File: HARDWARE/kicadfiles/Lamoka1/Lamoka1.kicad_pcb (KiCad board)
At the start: 2 copper layers, 61 parts, among them IC1 INA240A2DR, J1 2606-1108/010-000, J2 2606-1352, J3 USB_C_Receptacle_USB2.0_14P, J4 470531000, J5 2604-1103, J6 Male-Header, J7 Male-Header, SW1 B3F-4055, U1 RP2354A, U10 ADS7128IRTER, U2 AMS1117-3.3, U3 74AHCT1G125, U4 LM5122MH/NOPB, U7 TPS62160DSGR, U8 TMP235A2DBZR, U9 TMP235A2DBZR

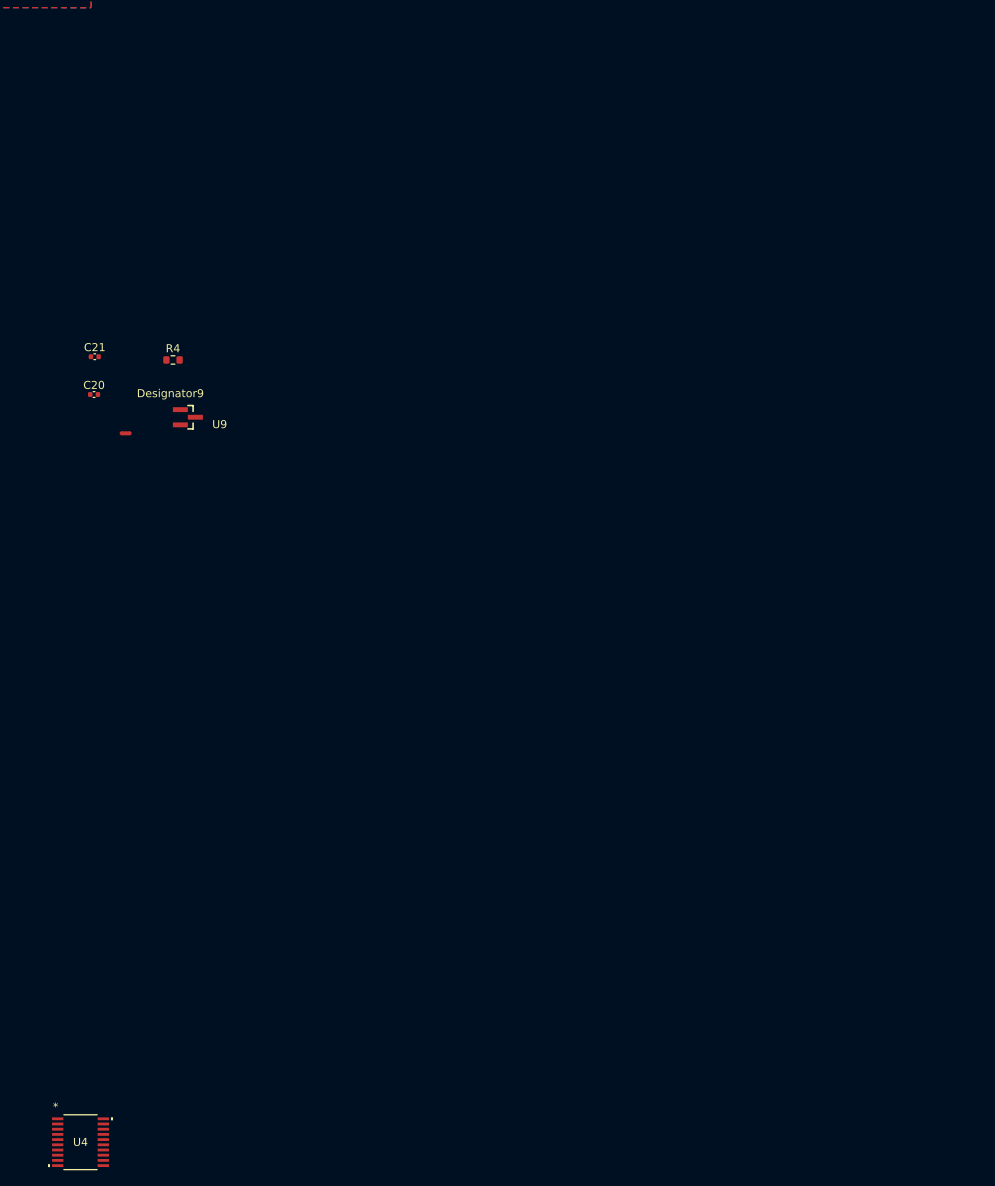
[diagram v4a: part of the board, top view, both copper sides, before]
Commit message: Route whole 11-14v to 17v boost converter
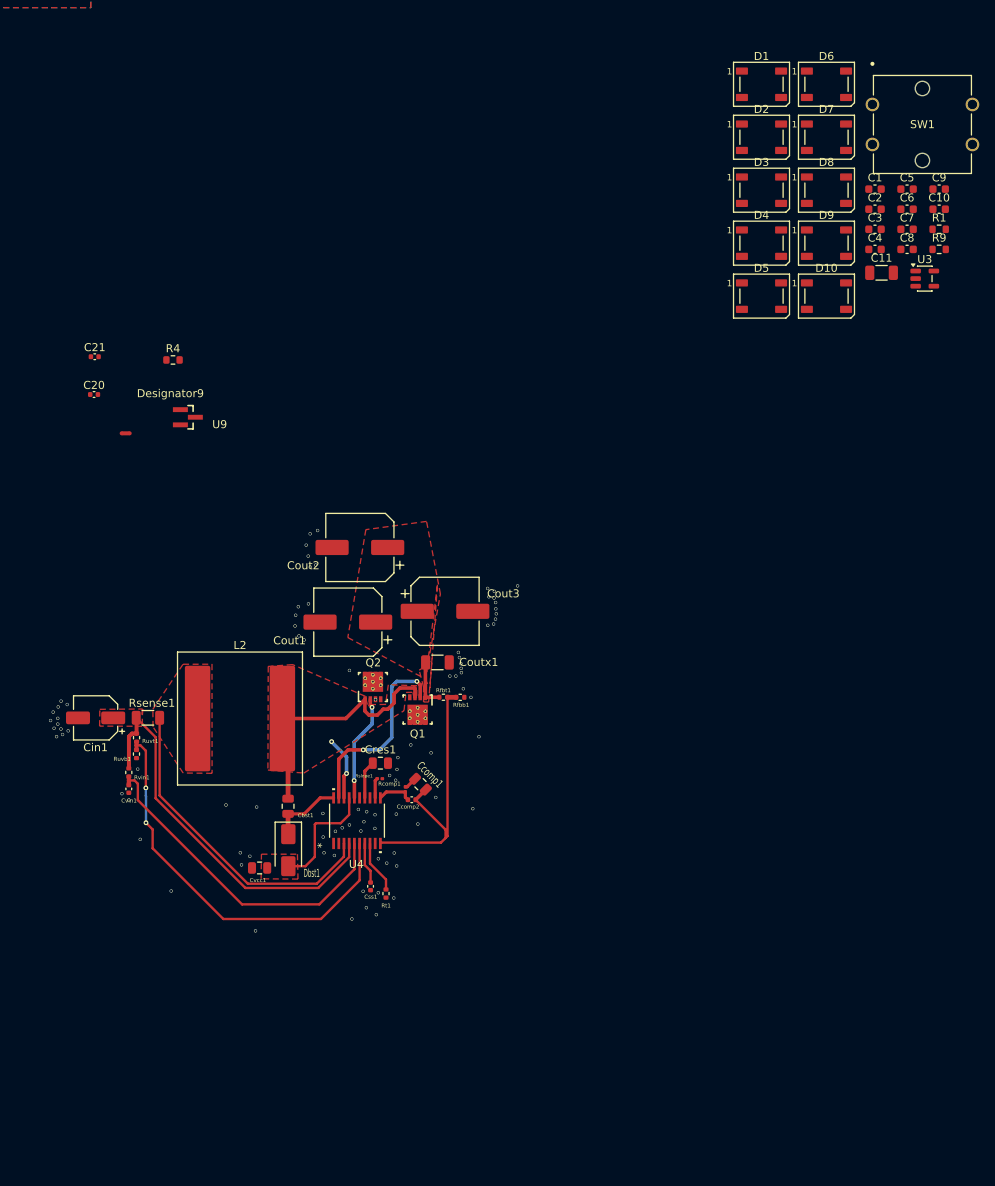
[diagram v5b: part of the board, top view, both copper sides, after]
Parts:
- added C1: 100n, Capacitor_SMD:C_0603_1608Metric, F.Cu at (246.3, 59.7)
- added C10: 100n, Capacitor_SMD:C_0603_1608Metric, F.Cu at (254.3, 62.2)
- added C11: 100u, Capacitor_SMD:C_1206_3216Metric, F.Cu at (247.1, 70.1)
- added C2: 100n, Capacitor_SMD:C_0603_1608Metric, F.Cu at (246.3, 62.2)
- added C3: 100n, Capacitor_SMD:C_0603_1608Metric, F.Cu at (246.3, 64.7)
- added C4: 100n, Capacitor_SMD:C_0603_1608Metric, F.Cu at (246.3, 67.2)
- added C5: 100n, Capacitor_SMD:C_0603_1608Metric, F.Cu at (250.3, 59.7)
- added C6: 100n, Capacitor_SMD:C_0603_1608Metric, F.Cu at (250.3, 62.2)
- added C7: 100n, Capacitor_SMD:C_0603_1608Metric, F.Cu at (250.3, 64.7)
- added C8: 100n, Capacitor_SMD:C_0603_1608Metric, F.Cu at (250.3, 67.2)
- added C9: 100n, Capacitor_SMD:C_0603_1608Metric, F.Cu at (254.3, 59.7)
- added Cbst1: 100nF, Capacitor_SMD:C_0805_2012Metric, F.Cu at (172.9, 136.8)
- added Ccomp1: 3.9nF, Capacitor_SMD:C_0805_2012Metric, F.Cu at (189.5, 134.0)
- added Ccomp2: 130pF, Capacitor_SMD:C_0402_1005Metric, F.Cu at (188.4, 136.0)
- added Cin1: 56uF, Capacitor_SMD:CP_Elec_5x5.9, F.Cu at (148.9, 125.8)
- added Cout1: 180uF, Capacitor_SMD:CP_Elec_8x11.9, F.Cu at (180.4, 113.8)
- added Cout2: 180uF, Capacitor_SMD:CP_Elec_8x11.9, F.Cu at (181.9, 104.5)
- added Cout3: 180uF, Capacitor_SMD:CP_Elec_8x11.9, F.Cu at (192.6, 112.4)
- added Coutx1: 47uF, Capacitor_SMD:C_1206_3216Metric, F.Cu at (191.6, 118.8)
- added Cres1: 470nF, Capacitor_SMD:C_0805_2012Metric, F.Cu at (184.5, 131.4)
- added Css1: 33nF, Capacitor_SMD:C_0402_1005Metric, F.Cu at (183.2, 146.8)
- added Cvcc1: 4.7uF, Capacitor_SMD:C_0805_2012Metric, F.Cu at (169.4, 144.5)
- added Cvin1: 470nF, Capacitor_SMD:C_0402_1005Metric, F.Cu at (153.0, 134.6)
- added D1: WS2812B, LED_SMD:LED_WS2812B_PLCC4_5.0x5.0mm_P3.2mm, F.Cu at (232.1, 46.5)
- added D10: WS2812B, LED_SMD:LED_WS2812B_PLCC4_5.0x5.0mm_P3.2mm, F.Cu at (240.2, 73.0)
- added D2: WS2812B, LED_SMD:LED_WS2812B_PLCC4_5.0x5.0mm_P3.2mm, F.Cu at (232.1, 53.2)
- added D3: WS2812B, LED_SMD:LED_WS2812B_PLCC4_5.0x5.0mm_P3.2mm, F.Cu at (232.1, 59.8)
- added D4: WS2812B, LED_SMD:LED_WS2812B_PLCC4_5.0x5.0mm_P3.2mm, F.Cu at (232.1, 66.4)
- added D5: WS2812B, LED_SMD:LED_WS2812B_PLCC4_5.0x5.0mm_P3.2mm, F.Cu at (232.1, 73.0)
- added D6: WS2812B, LED_SMD:LED_WS2812B_PLCC4_5.0x5.0mm_P3.2mm, F.Cu at (240.2, 46.5)
- added D7: WS2812B, LED_SMD:LED_WS2812B_PLCC4_5.0x5.0mm_P3.2mm, F.Cu at (240.2, 53.2)
- added D8: WS2812B, LED_SMD:LED_WS2812B_PLCC4_5.0x5.0mm_P3.2mm, F.Cu at (240.2, 59.8)
- added D9: WS2812B, LED_SMD:LED_WS2812B_PLCC4_5.0x5.0mm_P3.2mm, F.Cu at (240.2, 66.4)
- added Dbst1: D, Diode_SMD:D_SMA, F.Cu at (173.0, 142.3)
- added L2: 1.8uH, Inductor_SMD:L_Coilcraft_XAL1580-182, F.Cu at (166.9, 125.8)
- added Q1: 25V 60A N-Ch, CSD16323Q3:DQG0008A, F.Cu at (189.1, 124.7)
- added Q2: 30V 56A N-Ch, CSD17304Q3:DQG0008A, F.Cu at (183.5, 121.9)
- added R1: 330, Resistor_SMD:R_0603_1608Metric, F.Cu at (254.3, 64.7)
- added R9: 10k, Resistor_SMD:R_0603_1608Metric, F.Cu at (254.3, 67.2)
- added Rcomp1: 28.7k, Resistor_SMD:R_0201_0603Metric, F.Cu at (187.6, 134.7)
- added Rfbb1: 3.79k, Resistor_SMD:R_0402_1005Metric, F.Cu at (194.4, 123.2)
- added Rfbt1: 49.9k, Resistor_SMD:R_0402_1005Metric, F.Cu at (192.3, 123.2)
- added Rsense1: 2m, Resistor_SMD:R_1206_3216Metric, F.Cu at (155.4, 125.7)
- added Rslope1: 105k, Resistor_SMD:R_0201_0603Metric, F.Cu at (184.4, 133.3)
- added Rt1: 18.2k, Resistor_SMD:R_0402_1005Metric, F.Cu at (185.2, 147.7)
- added Ruvb1: 7.15k, Resistor_SMD:R_0402_1005Metric, F.Cu at (154.0, 130.3)
- added Ruvt1: 49.9k, Resistor_SMD:R_0402_1005Metric, F.Cu at (154.0, 128.2)
- added Rvin1: 3.01, Resistor_SMD:R_0402_1005Metric, F.Cu at (153.0, 132.6)
- added SW1: B3F-4055, B3F-4055:SW_B3F-4050_OMR, F.Cu at (246.0, 49.1)
- added U3: 74AHCT1G125, Package_TO_SOT_SMD:SOT-23-5, F.Cu at (252.5, 70.8)
- moved U4 53.0 mm to (181.5, 138.6), turned to 90 degrees
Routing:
- net /Inversion-Section/UVLO: track 0.00 -> 51.2 mm, vias 0 -> 2
- net /Inversion-Section/CSP: track 15.0 -> 66.1 mm
- net /Inversion-Section/VIN: track 0.00 -> 42.1 mm
- net /Inversion-Section/SW: track 0.00 -> 40.7 mm, vias 0 -> 2
- net /Inversion-Section/CSN: track 0.00 -> 40.4 mm
- net /Inversion-Section/FB: track 0.00 -> 35.4 mm
- net /Inversion-Section/HO: track 0.00 -> 24.5 mm, vias 0 -> 2
- net /Inversion-Section/VCC: track 0.00 -> 14.8 mm
- net /Inversion-Section/LO: track 0.00 -> 13.4 mm, vias 0 -> 2
- net /Inversion-Section/BST: track 0.00 -> 9.07 mm
- net /Inversion-Section/SYNCIN_RT: track 0.00 -> 6.58 mm
- net /Inversion-Section/G4D: track 0.00 -> 6.11 mm
- net /Inversion-Section/SS: track 0.00 -> 5.18 mm
- net /Inversion-Section/RES: track 0.00 -> 4.75 mm
- net /Inversion-Section/COMP: track 0.00 -> 4.53 mm
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- added copper zone on F.Cu, net /Inversion-Section/CSN
- added copper zone on F.Cu, net /Inversion-Section/CSP
- added copper zone on F.Cu, net /Inversion-Section/G4D
- added copper zone on F.Cu, net /Inversion-Section/SW
- added copper zone on F.Cu, net /Inversion-Section/VCC

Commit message: Route in pin header for user interface board, and put in connector for fan, other changes as well
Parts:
- removed the C1 at (246.3, 59.7)
- removed the C10 at (254.3, 62.2)
- removed the C11 at (247.1, 70.1)
- removed the C2 at (246.3, 62.2)
- removed the C3 at (246.3, 64.7)
- removed the C4 at (246.3, 67.2)
- removed the C5 at (250.3, 59.7)
- removed the C6 at (250.3, 62.2)
- removed the C7 at (250.3, 64.7)
- removed the C8 at (250.3, 67.2)
- removed the C9 at (254.3, 59.7)
- removed the D1 at (232.1, 46.5)
- removed the D10 at (240.2, 73.0)
- removed the D2 at (232.1, 53.2)
- removed the D3 at (232.1, 59.8)
- removed the D4 at (232.1, 66.4)
- removed the D5 at (232.1, 73.0)
- removed the D6 at (240.2, 46.5)
- removed the D7 at (240.2, 53.2)
- removed the D8 at (240.2, 59.8)
- removed the D9 at (240.2, 66.4)
- removed the R1 at (254.3, 64.7)
- removed the R9 at (254.3, 67.2)
- removed the SW1 at (246.0, 49.1)
- removed the U3 at (252.5, 70.8)
- moved C11 232.3 mm to (221.6, 171.7), turned to -90 degrees
- moved R9 224.6 mm to (217.1, 167.0), turned to 180 degrees
- moved SW1 221.9 mm to (201.6, 167.0), turned to 0 degrees
- moved J6 219.3 mm to (223.8, 161.8), turned to 0 degrees
- moved U3 210.9 mm to (215.8, 157.4), turned to 180 degrees
- moved R1 208.7 mm to (212.0, 156.4), turned to 0 degrees
- moved D1 204.4 mm to (207.6, 154.0), turned to -90 degrees
- moved C1 201.9 mm to (212.0, 151.5), turned to 0 degrees
- moved Cbst1 198.3 mm to (291.8, -21.9)
- moved Ccomp1 198.3 mm to (308.3, -24.7)
- moved Ccomp2 198.3 mm to (307.2, -22.8)
- moved Cin1 198.3 mm to (267.7, -33.0)
- moved Cout1 198.3 mm to (299.2, -45.0)
- moved Cout2 198.3 mm to (300.7, -54.3)
- moved Cout3 198.3 mm to (311.4, -46.3)
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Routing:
- net /Control-Section/AIN4: track 46.9 -> 2.22 mm
- net /GPIO5: track 0.00 -> 39.8 mm
- net /GPIO6: track 0.00 -> 35.7 mm
- net /Buck-5v: track 26.1 -> 5.20 mm
- net /Control-Section/GPIO11: track 9.68 -> 29.1 mm, vias 1 -> 3
- net /Control-Section/5V: track 45.9 -> 30.5 mm
- net /Control-Section/BTN: track 18.0 -> 29.6 mm
- net /Control-Section/TEMP_CTRL: track 0.00 -> 6.37 mm
- net /11-14V input: track 27.6 -> 23.0 mm
- net /Inversion-Section/CSP: track 66.1 -> 62.1 mm
- net /Control-Section/3v3: track 21.6 -> 19.9 mm
- added copper zone on F.Cu, net /Buck-5v
- added copper zone on F.Cu, net /Control-Section/3v3
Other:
- board outline added: 31.1 x 125.2 mm
- board text added: "FAN LAYOUT"
- board text added: "TRANSFORMER LAYOUT"
